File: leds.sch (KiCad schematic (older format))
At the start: 218 parts, among them U10 TLC5955, U11 TLC5955, U12 TLC5955, U13 TLC5955, U14 TLC5955, U15 TLC5955, U4 TLC5955, U5 TLC5955, U6 TLC5955, U7 TLC5955, U8 TLC5955, U9 TLC5955

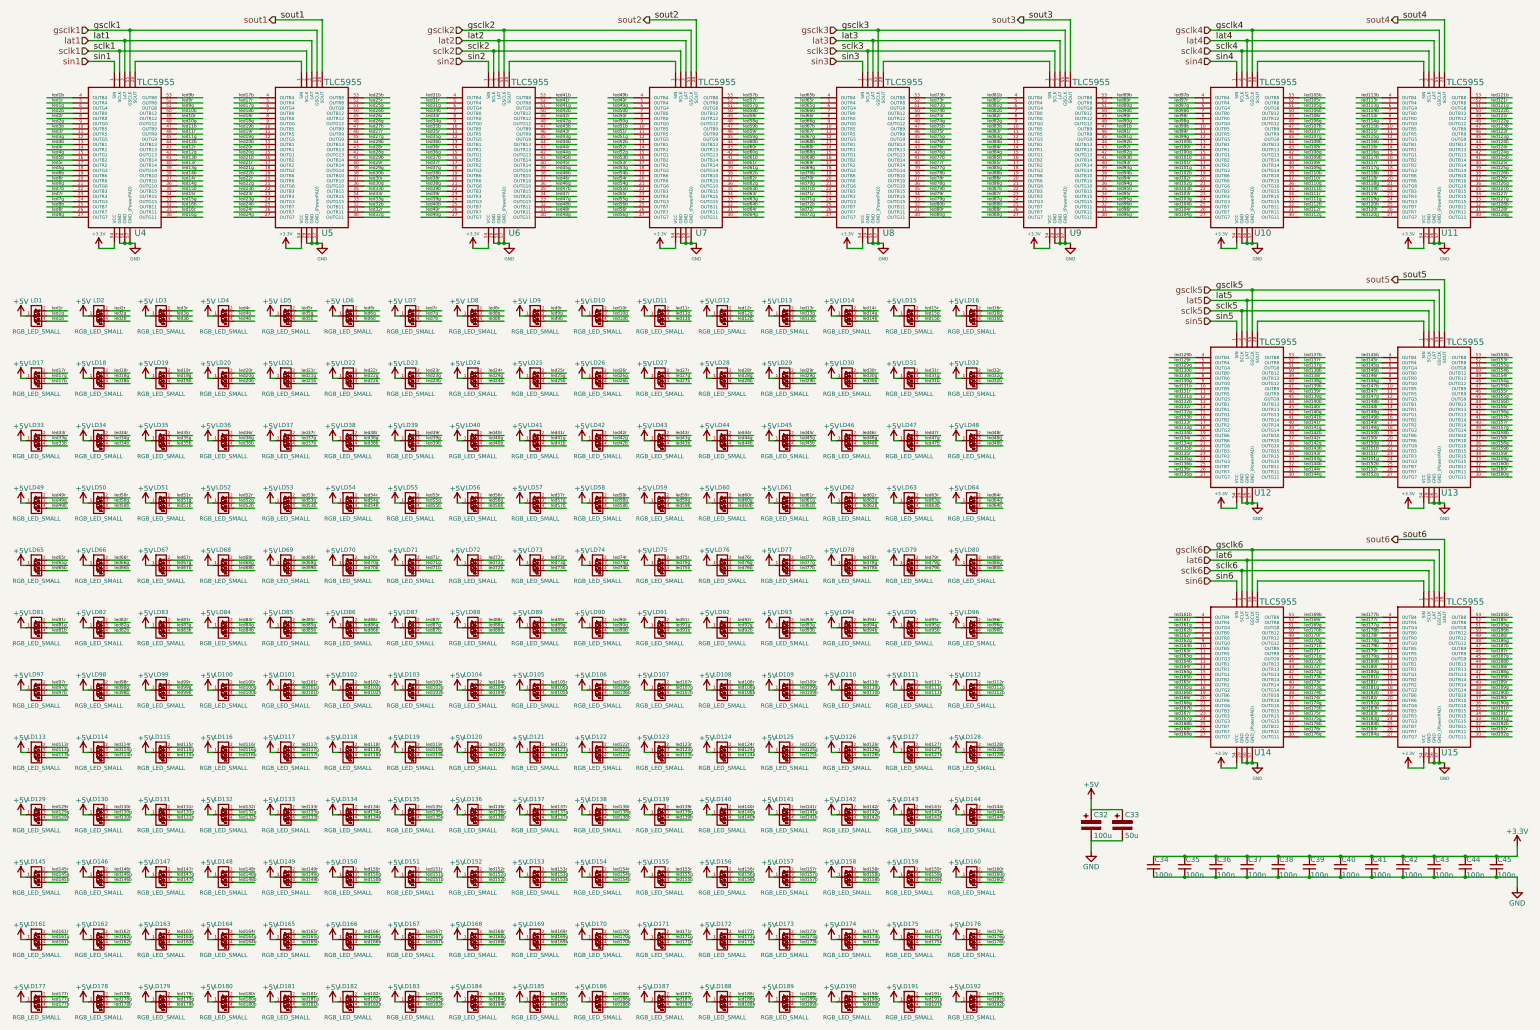
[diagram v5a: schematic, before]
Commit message: Some partial ideas for LEDs and TLCs placement and routing.
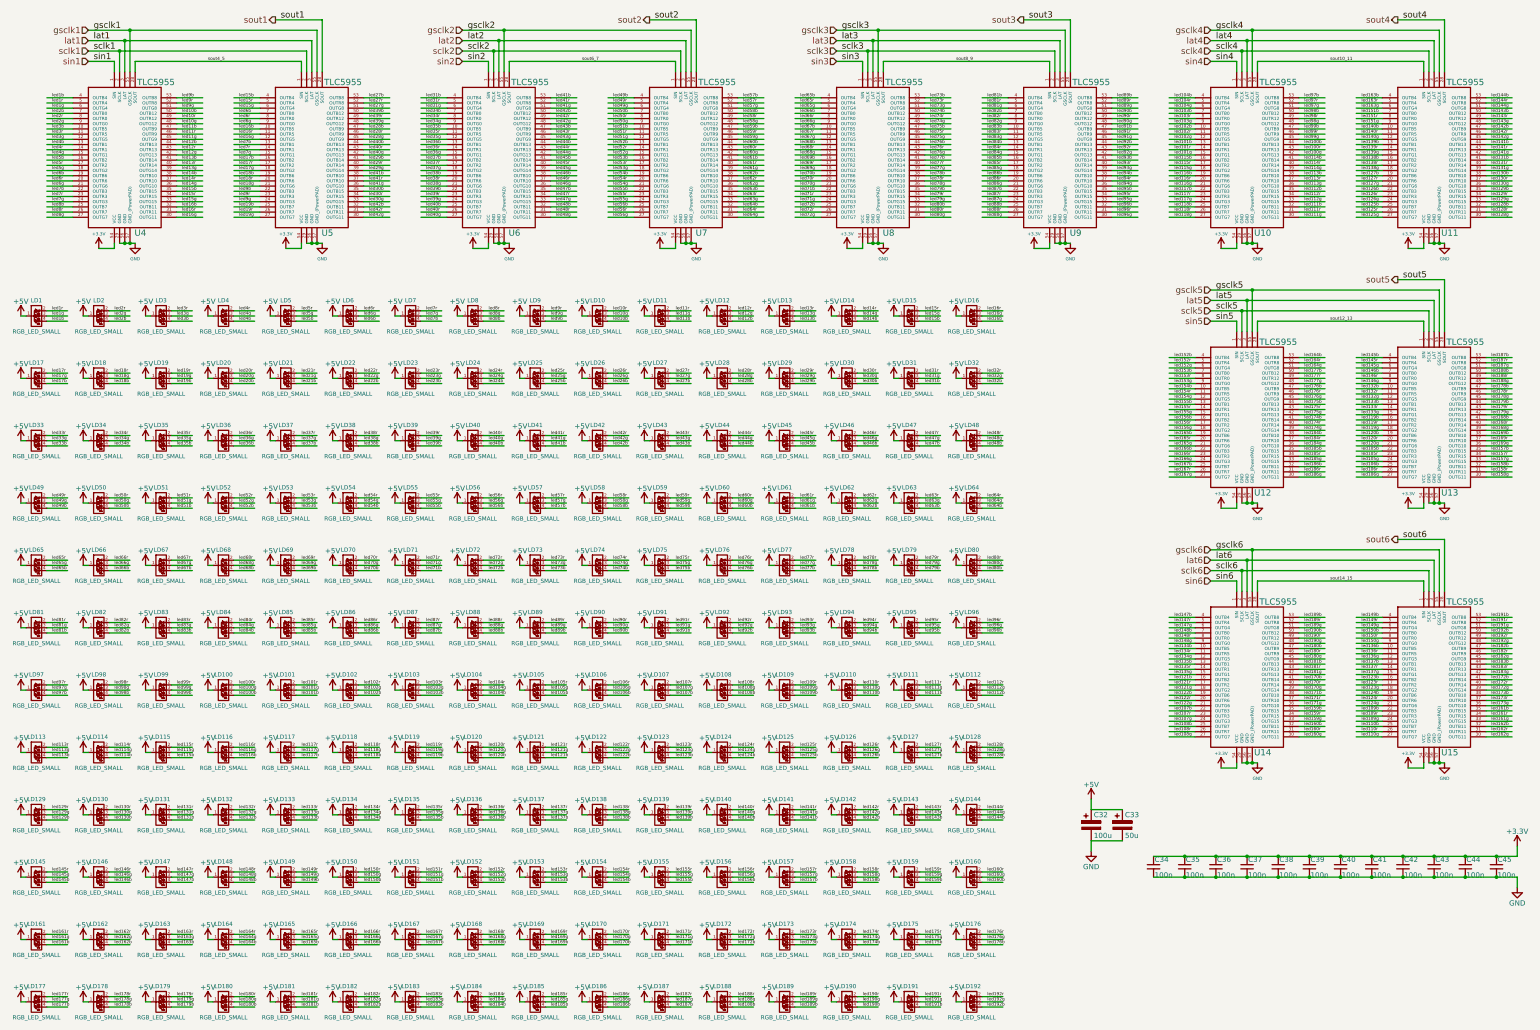
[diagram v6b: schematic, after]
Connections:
- net labels added: sout10_11, sout12_13, sout14_15, sout4_5, sout6_7, sout8_9

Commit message: Good progress on LED routing.
Upper half now routed with 6/6 mil tracks/clearance.
Still need to fit 5V vias for all LEDs, hopefully vias can find room.
Looks promising - if everything works, lower half should be doable the
same way.
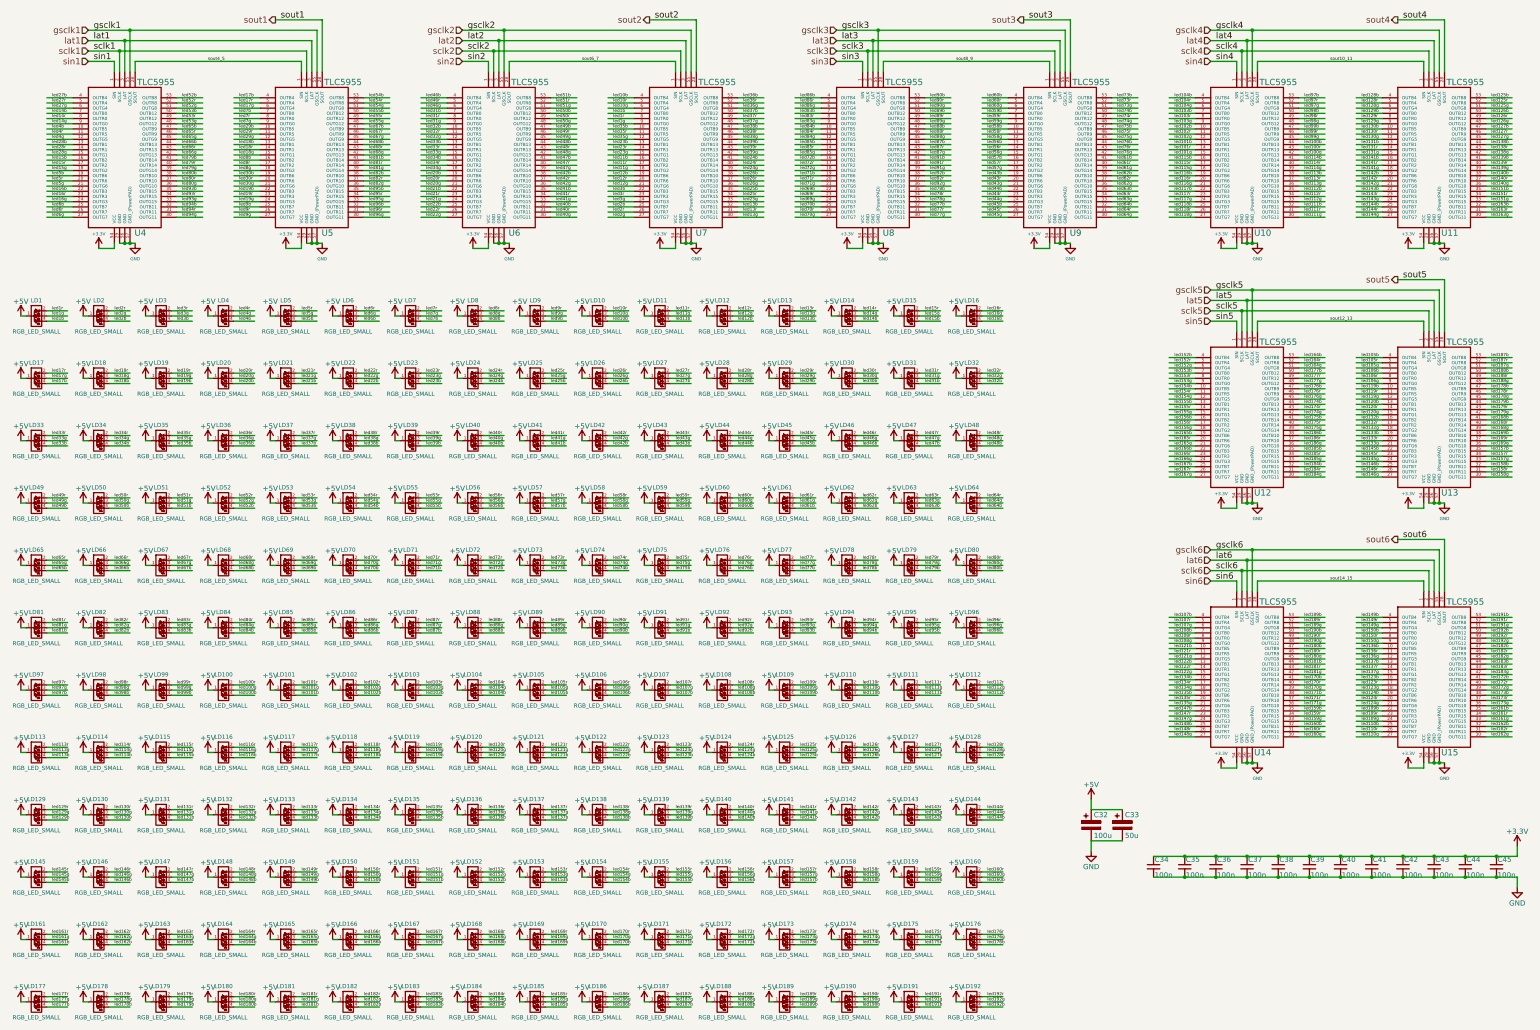
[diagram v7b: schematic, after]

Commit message: First reasonably complete routing of upper half of LEDs.
All LEDs have vias to power plane now. And TLCs have power and de-coupling.
Everything seems to fit, just.
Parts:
- C34, C35, C36, C37, C38, C39, C40, C41, C42, C43, C44, C45: footprint w_smd_cap:c_0805 -> w_smd_cap:c_0603
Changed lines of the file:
@@
 F 0 "C34" H 12110 9370 50  0000 L CNN
 F 1 "100n" H 12110 9220 50  0000 L CNN
-F 2 "w_smd_cap:c_0805" H 12100 9300 60  0001 C CNN
+F 2 "w_smd_cap:c_0603" H 12100 9300 60  0001 C CNN
 F 3 "" H 12100 9300 60  0000 C CNN
 	1    12100 9300
@@
 F 0 "C35" H 12410 9370 50  0000 L CNN
 F 1 "100n" H 12410 9220 50  0000 L CNN
-F 2 "w_smd_cap:c_0805" H 12400 9300 60  0001 C CNN
+F 2 "w_smd_cap:c_0603" H 12400 9300 60  0001 C CNN
 F 3 "" H 12400 9300 60  0000 C CNN
 	1    12400 9300
@@
 F 0 "C36" H 12710 9370 50  0000 L CNN
 F 1 "100n" H 12710 9220 50  0000 L CNN
-F 2 "w_smd_cap:c_0805" H 12700 9300 60  0001 C CNN
+F 2 "w_smd_cap:c_0603" H 12700 9300 60  0001 C CNN
 F 3 "" H 12700 9300 60  0000 C CNN
 	1    12700 9300
@@
 F 0 "C37" H 13010 9370 50  0000 L CNN
 F 1 "100n" H 13010 9220 50  0000 L CNN
-F 2 "w_smd_cap:c_0805" H 13000 9300 60  0001 C CNN
+F 2 "w_smd_cap:c_0603" H 13000 9300 60  0001 C CNN
 F 3 "" H 13000 9300 60  0000 C CNN
 	1    13000 9300
@@
 F 0 "C38" H 13310 9370 50  0000 L CNN
 F 1 "100n" H 13310 9220 50  0000 L CNN
-F 2 "w_smd_cap:c_0805" H 13300 9300 60  0001 C CNN
+F 2 "w_smd_cap:c_0603" H 13300 9300 60  0001 C CNN
 F 3 "" H 13300 9300 60  0000 C CNN
 	1    13300 9300
@@
 F 0 "C39" H 13610 9370 50  0000 L CNN
 F 1 "100n" H 13610 9220 50  0000 L CNN
-F 2 "w_smd_cap:c_0805" H 13600 9300 60  0001 C CNN
+F 2 "w_smd_cap:c_0603" H 13600 9300 60  0001 C CNN
 F 3 "" H 13600 9300 60  0000 C CNN
 	1    13600 9300
@@
 F 0 "C40" H 13910 9370 50  0000 L CNN
 F 1 "100n" H 13910 9220 50  0000 L CNN
-F 2 "w_smd_cap:c_0805" H 13900 9300 60  0001 C CNN
+F 2 "w_smd_cap:c_0603" H 13900 9300 60  0001 C CNN
 F 3 "" H 13900 9300 60  0000 C CNN
 	1    13900 9300
@@
 F 0 "C41" H 14210 9370 50  0000 L CNN
 F 1 "100n" H 14210 9220 50  0000 L CNN
-F 2 "w_smd_cap:c_0805" H 14200 9300 60  0001 C CNN
+F 2 "w_smd_cap:c_0603" H 14200 9300 60  0001 C CNN
 F 3 "" H 14200 9300 60  0000 C CNN
 	1    14200 9300
@@
 F 0 "C42" H 14510 9370 50  0000 L CNN
 F 1 "100n" H 14510 9220 50  0000 L CNN
-F 2 "w_smd_cap:c_0805" H 14500 9300 60  0001 C CNN
+F 2 "w_smd_cap:c_0603" H 14500 9300 60  0001 C CNN
 F 3 "" H 14500 9300 60  0000 C CNN
 	1    14500 9300
@@
 F 0 "C43" H 14810 9370 50  0000 L CNN
 F 1 "100n" H 14810 9220 50  0000 L CNN
-F 2 "w_smd_cap:c_0805" H 14800 9300 60  0001 C CNN
+F 2 "w_smd_cap:c_0603" H 14800 9300 60  0001 C CNN
 F 3 "" H 14800 9300 60  0000 C CNN
 	1    14800 9300
@@
 F 0 "C44" H 15110 9370 50  0000 L CNN
 F 1 "100n" H 15110 9220 50  0000 L CNN
-F 2 "w_smd_cap:c_0805" H 15100 9300 60  0001 C CNN
+F 2 "w_smd_cap:c_0603" H 15100 9300 60  0001 C CNN
 F 3 "" H 15100 9300 60  0000 C CNN
 	1    15100 9300
@@
 F 0 "C45" H 15410 9370 50  0000 L CNN
 F 1 "100n" H 15410 9220 50  0000 L CNN
-F 2 "w_smd_cap:c_0805" H 15400 9300 60  0001 C CNN
+F 2 "w_smd_cap:c_0603" H 15400 9300 60  0001 C CNN
 F 3 "" H 15400 9300 60  0000 C CNN
 	1    15400 9300
